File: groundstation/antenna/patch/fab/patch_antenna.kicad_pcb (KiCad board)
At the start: 2 copper layers, 160 x 160 mm, 0 parts

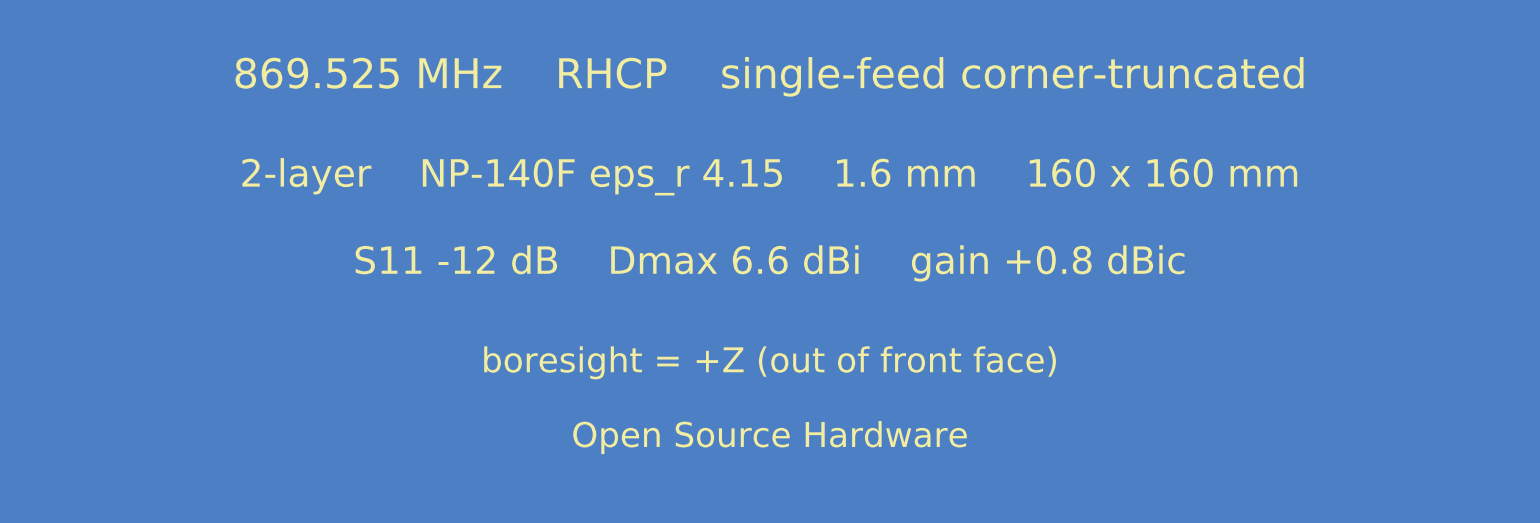
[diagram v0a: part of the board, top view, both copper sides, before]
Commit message: Patch antenna: sealed printable enclosure + 350k datasheet & thermal/trunc results
Squash of the enclosure + datasheet work on this branch:
- casing/: parametric OpenSCAD enclosure (rev C) - all-nylon standoffs, debossed
  branding + sunburst, beveled bezel + R10 corners, DFM/seal build-time asserts
- datasheet: 350k convergence-proven; 1.6mm corner truncation confirmed optimal
- record thermal CP-window + add thermal-drift and trunc-bw sweep tools/results
- archive old logos; add KiCad project file (fab/patch_antenna.kicad_pro)
- portability: deco_svg is now relative to the .scad (no host absolute path);
  ignore machine-local .mcp.json
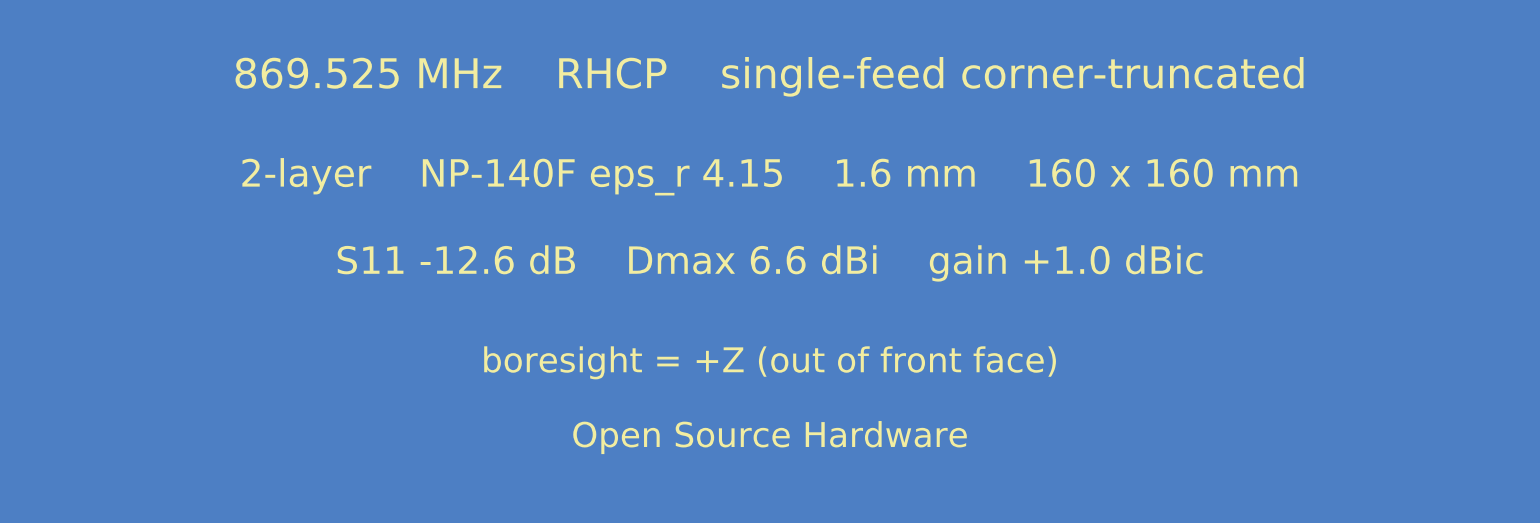
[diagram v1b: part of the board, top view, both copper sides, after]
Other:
- board text added: "-12.6 dB"
- board text added: "1.0 dB"
- board text added: "1.0 dBic"
- board text added: "AR over 45 deg cone"
- board text added: "Axial ratio (bore)"
- board text added: "S11 -12.6 dB Dmax 6.6 dBi gain +1.0 dBic"
- board text added: "worst 1.7 dB"
- board text removed: "-12.1 dB"
- board text removed: "0.8 dBic"
- board text removed: ">=45 deg cone (worst 1.0 dB)"
- board text removed: "AR<=3 coverage"
- board text removed: "Axial ratio"
- board text removed: "S11 -12 dB Dmax 6.6 dBi gain +0.8 dBic"
- board text removed: "~1.4 dB (band)"
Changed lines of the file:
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@@
     (effects (font (size 1.10 1.10) (thickness 0.154)))
   )
-  (gr_text "S11 -12 dB    Dmax 6.6 dBi    gain +0.8 dBic"
+  (gr_text "S11 -12.6 dB    Dmax 6.6 dBi    gain +1.0 dBic"
     (at 80.0000 26.0000) (layer "F.SilkS")
     (effects (font (size 1.10 1.10) (thickness 0.154)))
@@
     (effects (font (size 1.20 1.20) (thickness 0.168)) (justify mirror left))
   )
-  (gr_text "-12.1 dB"
+  (gr_text "-12.6 dB"
     (at 109.2000 68.4960) (layer "B.SilkS")
     (effects (font (size 1.20 1.20) (thickness 0.168)) (justify mirror left))
   )
-  (gr_text "Axial ratio"
+  (gr_text "Axial ratio (bore)"
     (at 145.2000 74.0960) (layer "B.SilkS")
     (effects (font (size 1.20 1.20) (thickness 0.168)) (justify mirror left))
   )
-  (gr_text "~1.4 dB (band)"
+  (gr_text "1.0 dB"
     (at 109.2000 74.0960) (layer "B.SilkS")
     (effects (font (size 1.20 1.20) (thickness 0.168)) (justify mirror left))
   )
-  (gr_text "AR<=3 coverage"
+  (gr_text "AR over 45 deg cone"
     (at 145.2000 79.6960) (layer "B.SilkS")
     (effects (font (size 1.20 1.20) (thickness 0.168)) (justify mirror left))
   )
-  (gr_text ">=45 deg cone (worst 1.0 dB)"
+  (gr_text "worst 1.7 dB"
     (at 109.2000 79.6960) (layer "B.SilkS")
     (effects (font (size 1.20 1.20) (thickness 0.168)) (justify mirror left))
@@
     (effects (font (size 1.20 1.20) (thickness 0.168)) (justify mirror left))
   )
-  (gr_text "0.8 dBic"
+  (gr_text "1.0 dBic"
     (at 109.2000 90.8960) (layer "B.SilkS")
     (effects (font (size 1.20 1.20) (thickness 0.168)) (justify mirror left))
